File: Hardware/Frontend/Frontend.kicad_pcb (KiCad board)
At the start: 4 copper layers, 50 x 48 mm, 138 parts, among them J1 Conn_Coaxial, J4 Conn_Coaxial, J5 Conn_Coaxial, J6 Conn_Coaxial, J7 Conn_Coaxial, U1 OPA145ID, U10 OPA145ID, U11 OPA145ID, U12 OPA145ID, U13 OPA145ID, U14 OPA145ID, U15 OPA145ID, U2 OPA145ID, U3 OPA145ID, U4 OPA145ID, U5 OPA145ID, U6 OPA145ID, U7 OPA145ID, U8 OPA145ID, U9 OPA145ID

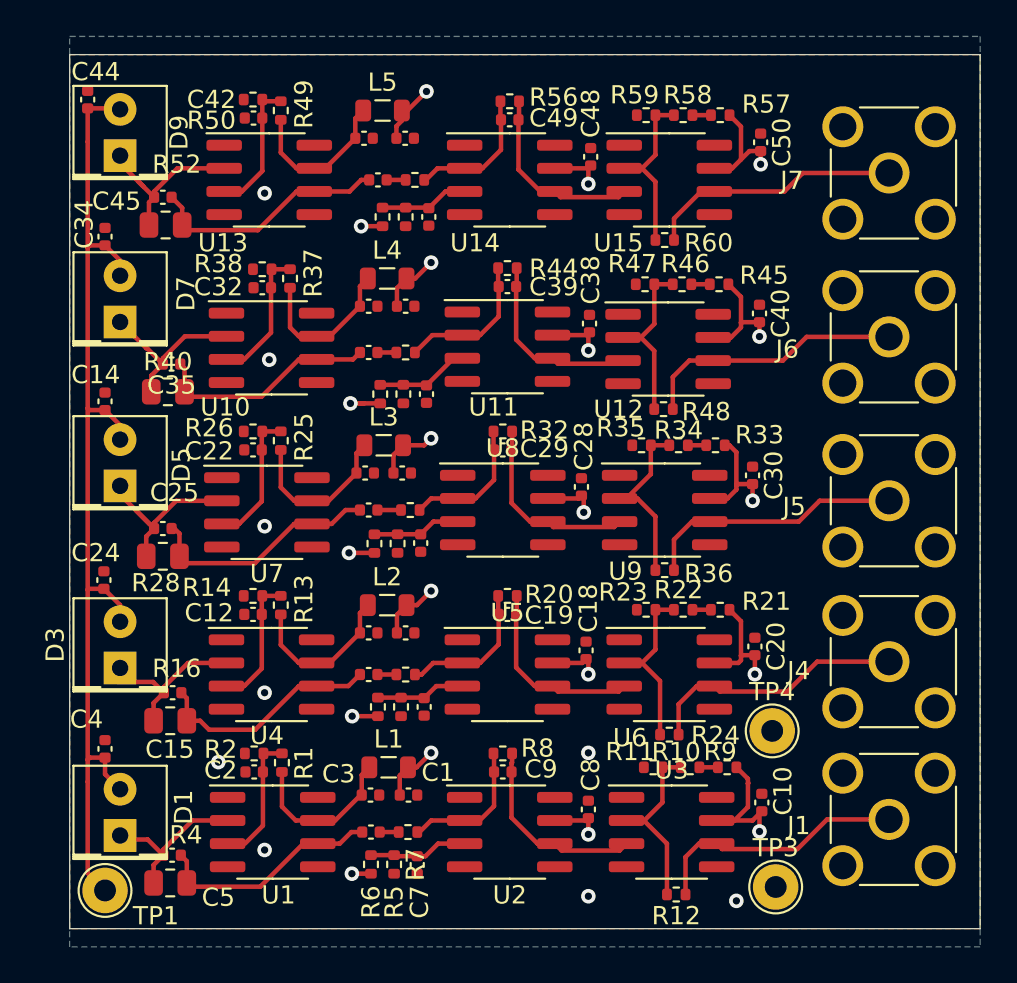
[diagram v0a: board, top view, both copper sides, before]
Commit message: add bom
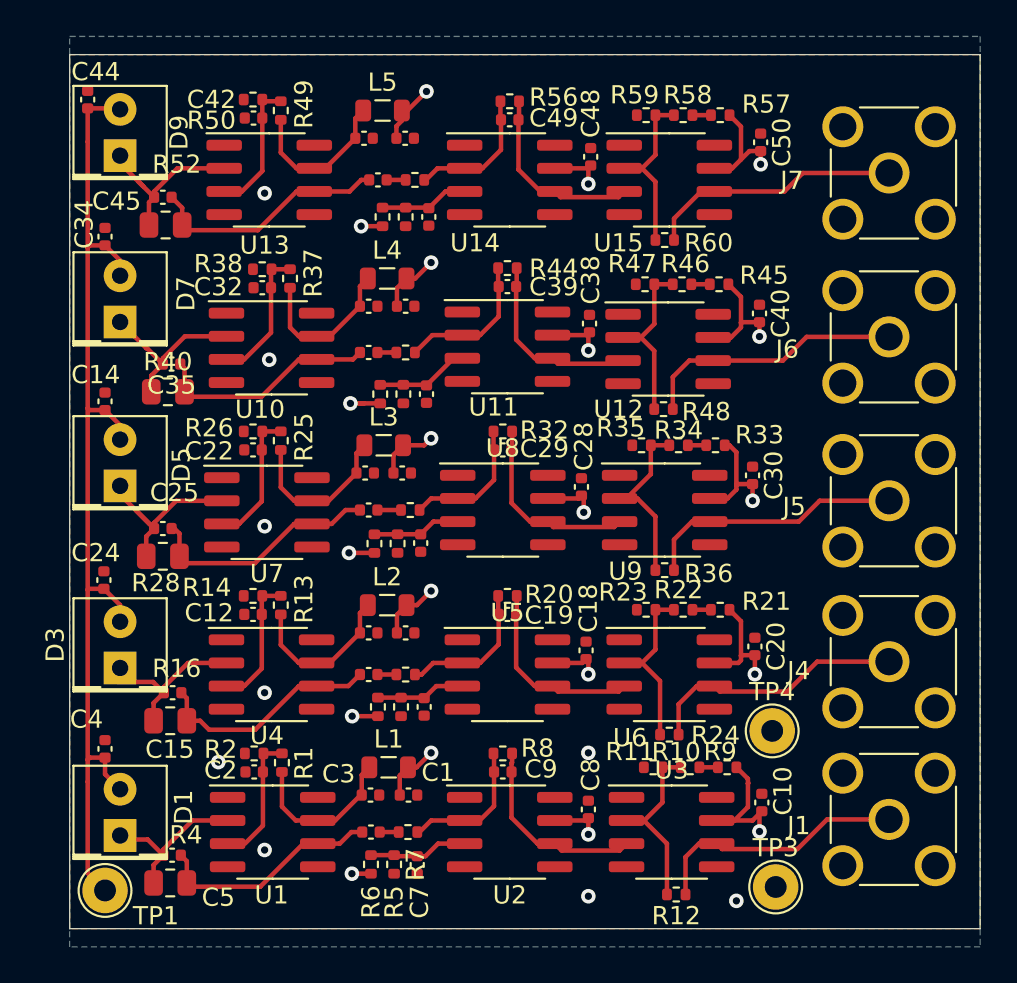
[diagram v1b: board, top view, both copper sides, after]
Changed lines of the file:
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@@
   (page A4)
   (layers
-    (0 F.Cu signal hide)
+    (0 F.Cu signal)
     (1 In1.Cu signal hide)
     (2 In2.Cu signal hide)
@@
     (tags "SOIC SO")
     (attr smd)
-    (fp_text reference U13 (at -2.54 3.461) (layer F.SilkS)
+    (fp_text reference U13 (at -0.254 3.588) (layer F.SilkS)
       (effects (font (size 1 1) (thickness 0.15)))
     )
@@
     (tags "SOIC SO")
     (attr smd)
-    (fp_text reference U10 (at -2.54 3.2545) (layer F.SilkS)
+    (fp_text reference U10 (at -0.635 3.3815) (layer F.SilkS)
       (effects (font (size 1 1) (thickness 0.15)))
     )
@@
     (tags "SOIC SO")
     (attr smd)
-    (fp_text reference U1 (at 0.3175 3.4605) (layer F.SilkS)
+    (fp_text reference U1 (at -0.0635 3.4605) (layer F.SilkS)
       (effects (font (size 1 1) (thickness 0.15)))
     )
